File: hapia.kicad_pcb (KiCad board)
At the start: 6 copper layers, 19 parts, among them J1 ATX-20, J3 Conn_01x04_Pin, J4 Conn_01x04_Pin, J5 Conn_01x04_Pin, J6 Conn_01x04_Pin, J7 Conn_01x15_Pin, J8 SUB_placa_de_controle, U1 STM32F407VETx, U2 TMC2209-LA, U3 TPS54302, U4 TMC2209-LA, U5 TMC2209-LA, U6 TMC2209-LA, U7 SRV05-4

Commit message: 21082026/G
falta muita coisa
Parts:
- moved U1 74.4 mm to (74.5, 74.3)

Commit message: 29082026/I
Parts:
- removed J1: ATX-20, Connector_Molex:Molex_Mini-Fit_Jr_5566-20A_2x10_P4.20mm_Vertical
- removed J8: SUB_placa_de_controle, Connector_PinHeader_2.54mm:PinHeader_1x10_P2.54mm_Vertical
- removed L1: 6.8uh, Inductor_SMD:L_Bourns_SRP1038C_10.0x10.0mm
- added C1: 22pf, Capacitor_SMD:C_0603_1608Metric_Pad1.08x0.95mm_HandSolder, F.Cu at (59.1, 84.2)
- added C12: 1µf, Capacitor_SMD:C_0805_2012Metric_Pad1.18x1.45mm_HandSolder, F.Cu at (78.6, 21.0)
- added C13: 100nf, Capacitor_SMD:C_0603_1608Metric, F.Cu at (38.9, 54.1)
- added C15: 22nf, Capacitor_SMD:C_0603_1608Metric_Pad1.08x0.95mm_HandSolder, F.Cu at (59.1, 89.2)
- added C16: 22nf, Capacitor_SMD:C_0603_1608Metric_Pad1.08x0.95mm_HandSolder, F.Cu at (59.1, 91.8)
- added C17: 100nf, Capacitor_SMD:C_0603_1608Metric, F.Cu at (38.9, 56.6)
- added C18: 100nf, Capacitor_SMD:C_0603_1608Metric, F.Cu at (38.9, 59.1)
- added C19: 100nf, Capacitor_SMD:C_0603_1608Metric, F.Cu at (38.9, 61.6)
- added C20: 100nf, Capacitor_SMD:C_0603_1608Metric, F.Cu at (38.9, 64.1)
- added C21: 1µf, Capacitor_SMD:C_0805_2012Metric_Pad1.18x1.45mm_HandSolder, F.Cu at (78.6, 24.0)
- added C22: 100nf, Capacitor_SMD:C_0603_1608Metric, F.Cu at (38.9, 66.6)
- added C23: 1µf, Capacitor_SMD:C_0805_2012Metric_Pad1.18x1.45mm_HandSolder, F.Cu at (78.6, 27.0)
- added C24: 100nf, Capacitor_SMD:C_0603_1608Metric, F.Cu at (42.9, 44.1)
- added C27: 1000µf, Capacitor_THT:CP_Radial_D12.5mm_P5.00mm, F.Cu at (27.4, 49.8)
- added C28: 100nf, Capacitor_SMD:C_0603_1608Metric, F.Cu at (42.9, 46.6)
- added C3: 100nf, Capacitor_SMD:C_0603_1608Metric, F.Cu at (38.9, 44.1)
- added C30: 100nf, Capacitor_SMD:C_0603_1608Metric, F.Cu at (42.9, 49.1)
- added C34: 1000µf, Capacitor_THT:CP_Radial_D12.5mm_P5.00mm, F.Cu at (27.4, 63.9)
- added C35: 22nf, Capacitor_SMD:C_0603_1608Metric_Pad1.08x0.95mm_HandSolder, F.Cu at (59.1, 94.3)
- added C36: 22nf, Capacitor_SMD:C_0603_1608Metric_Pad1.08x0.95mm_HandSolder, F.Cu at (59.1, 96.8)
- added C37: 100nf, Capacitor_SMD:C_0603_1608Metric, F.Cu at (42.9, 51.6)
- added C38: 100nf, Capacitor_SMD:C_0603_1608Metric, F.Cu at (42.9, 54.1)
- added C39: 100nf, Capacitor_SMD:C_0603_1608Metric, F.Cu at (42.9, 56.6)
- added C4: 100nf, Capacitor_SMD:C_0603_1608Metric, F.Cu at (38.9, 46.6)
- added C40: 100nf, Capacitor_SMD:C_0603_1608Metric, F.Cu at (42.9, 59.1)
- added C41: 1µf, Capacitor_SMD:C_0805_2012Metric_Pad1.18x1.45mm_HandSolder, F.Cu at (78.6, 30.0)
- added C42: 100nf, Capacitor_SMD:C_0603_1608Metric, F.Cu at (42.9, 61.6)
- added C43: 1µf, Capacitor_SMD:C_0805_2012Metric_Pad1.18x1.45mm_HandSolder, F.Cu at (78.6, 33.0)
- added C44: 100nf, Capacitor_SMD:C_0603_1608Metric, F.Cu at (42.9, 64.1)
- added C47: 100nf, Capacitor_SMD:C_0603_1608Metric, F.Cu at (42.9, 66.6)
- added C49: 100nf, Capacitor_SMD:C_0603_1608Metric, F.Cu at (46.9, 44.1)
- added C5: 22pf, Capacitor_SMD:C_0603_1608Metric_Pad1.08x0.95mm_HandSolder, F.Cu at (59.1, 86.7)
- added C54: 100nf, Capacitor_SMD:C_0603_1608Metric, F.Cu at (46.9, 46.6)
- added C56: 33nf, Capacitor_SMD:C_0402_1005Metric, F.Cu at (75.2, 89.7)
- added C57: 100nf, Capacitor_SMD:C_0603_1608Metric, F.Cu at (46.9, 49.1)
- added C58: 100nf, Capacitor_SMD:C_0603_1608Metric, F.Cu at (46.9, 51.6)
- added C59: 1000µf, Capacitor_THT:CP_Radial_D12.5mm_P5.00mm, F.Cu at (27.4, 77.9)
- added C60: 100nf, Capacitor_SMD:C_0603_1608Metric, F.Cu at (46.9, 54.1)
- added C61: 100nf, Capacitor_SMD:C_0603_1608Metric, F.Cu at (46.9, 56.6)
- added C63: 1µf, Capacitor_SMD:C_0805_2012Metric_Pad1.18x1.45mm_HandSolder, F.Cu at (78.6, 36.1)
- added C65: 100nf, Capacitor_SMD:C_0603_1608Metric, F.Cu at (46.9, 59.1)
- added C66: 1000µf, Capacitor_THT:CP_Radial_D12.5mm_P5.00mm, F.Cu at (27.4, 92.0)
- added C67: 100nf, Capacitor_SMD:C_0603_1608Metric, F.Cu at (46.9, 61.6)
- added C68: 100nf, Capacitor_SMD:C_0603_1608Metric, F.Cu at (46.9, 64.1)
- added C69: 100nf, Capacitor_SMD:C_0603_1608Metric, F.Cu at (46.9, 66.6)
- added C7: 100nf, Capacitor_SMD:C_0603_1608Metric, F.Cu at (38.9, 49.1)
- added C70: 100nf, Capacitor_SMD:C_0603_1608Metric, F.Cu at (50.9, 44.1)
- added C71: 100nf, Capacitor_SMD:C_0603_1608Metric, F.Cu at (50.9, 46.6)
- added C72: 100nf, Capacitor_SMD:C_0603_1608Metric, F.Cu at (50.9, 49.1)
- added C76: 100nf, Capacitor_SMD:C_0603_1608Metric, F.Cu at (50.9, 51.6)
- added C78: 100nf, Capacitor_SMD:C_0603_1608Metric, F.Cu at (50.9, 54.1)
- added C87: 100nf, Capacitor_SMD:C_0603_1608Metric, F.Cu at (50.9, 56.6)
- added C88: 100nf, Capacitor_SMD:C_0603_1608Metric, F.Cu at (50.9, 59.1)
- added C89: 100nf, Capacitor_SMD:C_0603_1608Metric, F.Cu at (50.9, 61.6)
- added C9: 100nf, Capacitor_SMD:C_0603_1608Metric, F.Cu at (38.9, 51.6)
- added C90: 100nf, Capacitor_SMD:C_0603_1608Metric, F.Cu at (50.9, 64.1)
- added C92: 100nf, Capacitor_SMD:C_0603_1608Metric, F.Cu at (50.9, 66.6)
- added C93: 100nf, Capacitor_SMD:C_0603_1608Metric, F.Cu at (54.9, 44.1)
- added C94: 100nf, Capacitor_SMD:C_0603_1608Metric, F.Cu at (54.9, 46.6)
- added CN1: 100nf, Capacitor_SMD:C_0603_1608Metric, F.Cu at (54.9, 49.1)
- added CN2: 100nf, Capacitor_SMD:C_0603_1608Metric, F.Cu at (54.9, 51.6)
- added CN3: 100nf, Capacitor_SMD:C_0603_1608Metric, F.Cu at (54.9, 54.1)
- added D1: SMF33A, Diode_SMD:D_SMF, F.Cu at (90.6, 69.2)
- added D3: SMF5V0A, Diode_SMD:D_SMF, F.Cu at (90.6, 72.5)
- added D4: SMF5V0A, Diode_SMD:D_SMF, F.Cu at (90.6, 75.9)
- added D7: SMF5V0A, Diode_SMD:D_SMF, F.Cu at (90.6, 79.2)
- added D8: SMF15A, Diode_SMD:D_SMF, F.Cu at (90.6, 82.6)
- added D9: SMF5V0A, Diode_SMD:D_SMF, F.Cu at (90.6, 85.9)
- added FB3: FerriteBead, Inductor_SMD:L_0805_2012Metric, F.Cu at (76.0, 87.4)
- added J17: Conn_01x04_MountingPin, Connector_JST:JST_SH_SM04B-SRSS-TB_1x04-1MP_P1.00mm_Horizontal, F.Cu at (92.1, 91.4)
- added J9: Conn_01x15_Pin, Connector_PinHeader_2.54mm:PinHeader_1x15_P2.54mm_Vertical, F.Cu at (59.2, 45.1)
- added JP1: usb/atx, Jumper:SolderJumper-3_P1.3mm_Bridged2Bar12_RoundedPad1.0x1.5mm, F.Cu at (39.7, 96.8)
- added JP2: fre, Jumper:SolderJumper-2_P1.3mm_Open_TrianglePad1.0x1.5mm, F.Cu at (44.7, 96.8)
- added R59: 100mΩ, Resistor_SMD:R_1206_3216Metric, F.Cu at (50.5, 69.6)
- added R60: 100mΩ, Resistor_SMD:R_1206_3216Metric, F.Cu at (50.5, 72.9)
- added R61: 100mΩ, Resistor_SMD:R_1206_3216Metric, F.Cu at (50.5, 76.2)
- added R62: 100mΩ, Resistor_SMD:R_1206_3216Metric, F.Cu at (50.5, 79.5)
- added R67: 100mΩ, Resistor_SMD:R_1206_3216Metric, F.Cu at (50.5, 82.8)
- added R68: 100mΩ, Resistor_SMD:R_1206_3216Metric, F.Cu at (50.5, 86.1)
- added R69: 100mΩ, Resistor_SMD:R_1206_3216Metric, F.Cu at (50.5, 89.4)
- added R70: 100mΩ, Resistor_SMD:R_1206_3216Metric, F.Cu at (50.5, 92.7)
- added TP10: 3.3v_power, TestPoint:TestPoint_Pad_D1.0mm, F.Cu at (69.2, 90.6)
- added TP11: 12v_power, TestPoint:TestPoint_Pad_D1.0mm, F.Cu at (69.2, 93.6)
- added TP12: 12v_power, TestPoint:TestPoint_Pad_D1.0mm, F.Cu at (69.2, 96.7)
- added TP13: TestPoint, TestPoint:TestPoint_Pad_D1.0mm, F.Cu at (72.2, 87.5)
- added TP14: 12v, TestPoint:TestPoint_Pad_D1.0mm, F.Cu at (72.2, 90.6)
- added TP15: 5v, TestPoint:TestPoint_Pad_D1.0mm, F.Cu at (72.2, 93.6)
- added TP16: 3.3v, TestPoint:TestPoint_Pad_D1.0mm, F.Cu at (72.2, 96.7)
- added TP5: 3.3v_power, TestPoint:TestPoint_Pad_D1.0mm, F.Cu at (66.1, 87.5)
- added TP6: 3.3v_power, TestPoint:TestPoint_Pad_D1.0mm, F.Cu at (66.1, 90.6)
- added TP7: 12v_power, TestPoint:TestPoint_Pad_D1.0mm, F.Cu at (66.1, 93.6)
- added TP8: 12v_power, TestPoint:TestPoint_Pad_D1.0mm, F.Cu at (66.1, 96.7)
- added TP9: 3.3v_power, TestPoint:TestPoint_Pad_D1.0mm, F.Cu at (69.2, 87.5)
- added U10: 74HC4051, Package_DIP:DIP-16_W7.62mm, F.Cu at (38.5, 69.9)
- added U11: UCC27524DR, Package_SO:SOIC-8_3.9x4.9mm_P1.27mm, F.Cu at (85.2, 22.9)
- added U12: UCC27524D, Package_SO:SOIC-8_3.9x4.9mm_P1.27mm, F.Cu at (85.2, 29.4)
- added U13: IRFS7530TRL7PP, Package_TO_SOT_SMD:TO-263-7_TabPin4, F.Cu at (72.3, 49.0)
- added U14: IRFS7530TRL7PP, Package_TO_SOT_SMD:TO-263-7_TabPin4, F.Cu at (72.3, 61.3)
- added U8: TPS62933F, Package_TO_SOT_SMD:SOT-583-8, F.Cu at (78.0, 39.6)
- added U9: SRV05-4, Package_TO_SOT_SMD:SOT-23-6, F.Cu at (93.4, 39.7)
- added Y1: 8mhz, Crystal:Crystal_SMD_5032-2Pin_5.0x3.2mm_HandSoldering, F.Cu at (42.1, 92.4)
- J7: value Conn_01x15_Pin -> ATX-24; footprint Connector_PinSocket_2.54mm:PinSocket_1x15_P2.54mm_Vertical -> Connector_Molex:Molex_Mini-Fit_Jr_5569-24A2_2x12_P4.20mm_Horizontal
- TP1, TP2, TP4: footprint Connector_USB:USB_Micro-B_Amphenol_10104110_Horizontal -> TestPoint:TestPoint_Pad_D1.0mm
- TP3: value TestPoint -> 3.3v; footprint Connector_USB:USB_Micro-B_Amphenol_10104110_Horizontal -> TestPoint:TestPoint_Pad_D1.0mm
- U1: value STM32F407VETx -> STM32F407VET6
- U2: value TMC2209-LA -> AMS1117-3.3; footprint Package_DFN_QFN:VQFN-28-1EP_5x5mm_P0.5mm_EP3.7x3.7mm_ThermalVias -> Package_TO_SOT_SMD:SOT-223-3_TabPin2
- U3: value TPS54302 -> SRV05-4
- U7: value SRV05-4 -> TMC2209-LA; footprint Package_TO_SOT_SMD:SOT-23-6 -> Package_DFN_QFN:VQFN-28-1EP_5x5mm_P0.5mm_EP3.7x3.7mm_ThermalVias
- moved U4 68.6 mm to (84.0, 71.1)
- moved U5 68.6 mm to (84.0, 78.4)
- moved U6 68.6 mm to (84.0, 85.6)
- moved TP1 66.8 mm to (63.1, 87.5)
- moved U1 64.9 mm to (139.0, 80.8), turned to 45 degrees
- moved TP2 64.4 mm to (63.1, 90.6)
- moved TP3 62.5 mm to (63.1, 93.6)
- moved U7 61.4 mm to (84.0, 92.9)
- moved U2 61.0 mm to (85.9, 36.9)
- moved TP4 60.9 mm to (63.1, 96.7)
- moved J3 54.2 mm to (82.8, 45.4)
- moved J4 54.2 mm to (82.8, 51.3)
- moved J5 54.2 mm to (82.8, 57.1)
- moved J6 54.2 mm to (82.8, 63.0)
- moved U3 49.2 mm to (93.4, 35.1)
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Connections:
- net Net-(U1-PA7) renamed SUB_RMII_CRS_DV
- net Net-(U3-BOOT) renamed USB_C_D-
- net Net-(U3-FB) renamed USB_C_D+
- net exrtusora renamed SWD_SWO
- net gpi_4 renamed Net-(J7-+5VSB)
- net gpi_5 renamed ATX_PWR
- J7 pad 1: GND -> unconnected-(J7-+3.3V-Pad1)_2
- J7 pad 10: gpi_3 -> hotbed
- J7 pad 11: gpi_2 -> hotbed
- J7 pad 12: gpi_1 -> unconnected-(J7-+3.3V-Pad1)_3
- J7 pad 13: +5V -> unconnected-(J7-+3.3V-Pad1)
- J7 pad 14: Net-(J7-Pin_14) -> unconnected-(J7--12V-Pad14)
- J7 pad 15: +12V -> GND
- J7 pad 2: STM_ADC -> unconnected-(J7-+3.3V-Pad1)_1
- J7 pad 3: STM_ADC_1 -> GND
- J7 pad 4: GND -> Net-(F7-Pad1)
- J7 pad 5: gpi_8 -> GND
- J7 pad 6: gpi_7 -> Net-(F7-Pad1)
- J7 pad 7: gpi_6 -> GND
- TP1 pad 1: 3.3v/1 -> STM_boot
- TP2 pad 1: 3.3v/1 -> STM_nrst
- TP4 pad 1: +12V -> Net-(D2-A)
- U1 pad 1: unconnected-(U1-PE2-Pad1) -> Net-(U1-PE2)
- U1 pad 14: 3.3v/1 -> STM_nrst
- U1 pad 15: unconnected-(U1-PC0-Pad15) -> NTC_MUX_out
- U1 pad 17: unconnected-(U1-PC2-Pad17) -> Net-(RN4A-R1.2)
- U1 pad 18: unconnected-(U1-PC3-Pad18) -> Net-(RN4B-R2.2)
- U1 pad 2: unconnected-(U1-PE3-Pad2) -> Net-(U1-PE3)
- U1 pad 21: 3.3v/A -> VDDA
- U1 pad 22: Net-(U1-VDDA) -> VDDA
- U1 pad 3: unconnected-(U1-PE4-Pad3) -> Net-(U1-PE4)
- U1 pad 36: unconnected-(U1-PB1-Pad36) -> SWD/jtag_rst
- U1 pad 38: unconnected-(U1-PE7-Pad38) -> Net-(RN3A-R1.1)
- U1 pad 39: unconnected-(U1-PE8-Pad39) -> Net-(RN3B-R2.1)
- U1 pad 4: unconnected-(U1-PE5-Pad4) -> Net-(U1-PE5)
- U1 pad 40: unconnected-(U1-PE9-Pad40) -> Net-(RN3C-R3.1)
- U1 pad 41: unconnected-(U1-PE10-Pad41) -> Net-(RN3D-R4.1)
- U1 pad 42: unconnected-(U1-PE11-Pad42) -> Net-(RN3E-R5.1)
- U1 pad 43: unconnected-(U1-PE12-Pad43) -> Net-(RN3F-R6.1)
- U1 pad 44: unconnected-(U1-PE13-Pad44) -> Net-(RN3G-R7.1)
- U1 pad 45: unconnected-(U1-PE14-Pad45) -> Net-(RN3H-R8.1)
- U1 pad 46: unconnected-(U1-PE15-Pad46) -> Net-(U1-PE15)
- U1 pad 48: unconnected-(U1-PB11-Pad48) -> Net-(U1-PB11)
- U1 pad 5: unconnected-(U1-PE6-Pad5) -> Net-(U1-PE6)
- U1 pad 51: unconnected-(U1-PB12-Pad51) -> Net-(U1-PB12)
- U1 pad 52: unconnected-(U1-PB13-Pad52) -> Net-(U1-PB13)
- U1 pad 55: unconnected-(U1-PD8-Pad55) -> NTC_MUX_0
- U1 pad 56: unconnected-(U1-PD9-Pad56) -> NTC_MUX_1
- U1 pad 57: unconnected-(U1-PD10-Pad57) -> NTC_MUX_2
- U1 pad 61: unconnected-(U1-PD14-Pad61) -> Net-(U1-PD14)
- U1 pad 62: unconnected-(U1-PD15-Pad62) -> Net-(U1-PD15)
- U1 pad 63: unconnected-(U1-PC6-Pad63) -> Net-(RN4E-R5.2)
- U1 pad 64: unconnected-(U1-PC7-Pad64) -> Net-(RN4F-R6.2)
- U1 pad 65: unconnected-(U1-PC8-Pad65) -> Net-(RN4G-R7.2)
- U1 pad 66: unconnected-(U1-PC9-Pad66) -> Net-(RN4H-R8.2)
- U1 pad 70: unconnected-(U1-PA11-Pad70) -> gpi_PD14
- U1 pad 71: unconnected-(U1-PA12-Pad71) -> gpi_PD15
- U1 pad 72: unconnected-(U1-PA13-Pad72) -> Net-(U1-PA13)
- U1 pad 76: unconnected-(U1-PA14-Pad76) -> Net-(U1-PA14)
- U1 pad 77: Net-(U1-PA15) -> unconnected-(U1-PA15-Pad77)
- U1 pad 78: Net-(U1-PC10) -> unconnected-(U1-PC10-Pad78)
- U1 pad 79: Net-(U1-PC11) -> unconnected-(U1-PC11-Pad79)
- U1 pad 91: SUB_2 -> Net-(RN1G-R7.2)
- U1 pad 92: SUB_3 -> Net-(RN1F-R6.2)
- U1 pad 93: SUB_4 -> Net-(RN1E-R5.2)
- U1 pad 94: 3.3v/1 -> STM_boot
- U1 pad 95: SUB_5 -> Net-(RN1D-R4.2)
- U1 pad 96: SUB_6 -> Net-(RN1C-R3.2)
- U1 pad 97: unconnected-(U1-PE0-Pad97) -> Net-(RN1A-R1.1)
- U1 pad 98: unconnected-(U1-PE1-Pad98) -> Net-(RN1B-R2.1)
- U2 pad 1: Net-(J3-Pin_1) -> GND
- U2 pad 2: Net-(U2-~{EN}) -> +3.3Vdev
- U2 pad 3: GND -> +5Vusb
- U3 pad 1: GND -> unconnected-(U3-IO1-Pad1)
- U3 pad 2: Net-(U3-SW) -> Net-(D2-A)
- U3 pad 3: Net-(U3-VIN) -> unconnected-(U3-IO2-Pad3)
- U3 pad 5: unconnected-(U3-EN-Pad5) -> GND
- U4 pad 1: Net-(J4-Pin_1) -> Net-(J3-Pin_1)
- U4 pad 10: TMC_MS2_3 -> GND
- U4 pad 14: TMC_uart3 -> TMC_uart
- U4 pad 15: 3.3v/1 -> +3V3
- U4 pad 16: unconnected-(U4-STEP-Pad16) -> TMC_step_1
- U4 pad 17: unconnected-(U4-VREF-Pad17) -> Net-(U4-VREF)
- U4 pad 19: unconnected-(U4-DIR-Pad19) -> TMC_DIR_1
- U4 pad 21: Net-(J4-Pin_3) -> Net-(J3-Pin_3)
- U4 pad 22: +12V -> +12P
- U4 pad 24: Net-(J4-Pin_4) -> Net-(J3-Pin_4)
- U4 pad 26: Net-(J4-Pin_2) -> Net-(J3-Pin_2)
- U4 pad 28: +12V -> +12P
- U4 pad 6: TMC_3vcp -> Net-(U4-VCP)
- U4 pad 8: TMC_3vut -> Net-(U4-5VOUT)
- U4 pad 9: TMC_MS1_3 -> GND
- U5 pad 1: Net-(J5-Pin_1) -> Net-(J4-Pin_1)
- U5 pad 10: TMC_MS2_4 -> GND
- U5 pad 14: TMC_uart4 -> TMC_uart
- U5 pad 15: 3.3v/1 -> +3V3
- U5 pad 16: unconnected-(U5-STEP-Pad16) -> TMC_step_3
- U5 pad 17: unconnected-(U5-VREF-Pad17) -> Net-(U5-VREF)
- U5 pad 19: unconnected-(U5-DIR-Pad19) -> TMC_DIR_3
- U5 pad 21: Net-(J5-Pin_3) -> Net-(J4-Pin_3)
- U5 pad 22: +12V -> +12P
- U5 pad 24: Net-(J5-Pin_4) -> Net-(J4-Pin_4)
- U5 pad 26: Net-(J5-Pin_2) -> Net-(J4-Pin_2)
- U5 pad 28: +12V -> +12P
- U5 pad 6: TMC_4vcp -> Net-(U5-VCP)
- U5 pad 8: TMC_4vut -> Net-(U5-5VOUT)
- U5 pad 9: TMC_MS1_4 -> +3V3
- U6 pad 1: Net-(J6-Pin_1) -> Net-(J5-Pin_1)
- U6 pad 10: TMC_MS2_2 -> +3V3
- U6 pad 14: TMC_uart2 -> TMC_uart
- U6 pad 15: 3.3v/1 -> +3V3
- U6 pad 16: unconnected-(U6-STEP-Pad16) -> TMC_step_2
- U6 pad 17: unconnected-(U6-VREF-Pad17) -> Net-(U6-VREF)
- U6 pad 19: unconnected-(U6-DIR-Pad19) -> TMC_DIR_2
- U6 pad 21: Net-(J6-Pin_3) -> Net-(J5-Pin_3)
- U6 pad 22: +12V -> +12P
- U6 pad 24: Net-(J6-Pin_4) -> Net-(J5-Pin_4)
- U6 pad 26: Net-(J6-Pin_2) -> Net-(J5-Pin_2)
- U6 pad 28: +12V -> +12P
- U6 pad 6: TMC_2vcp -> Net-(U6-VCP)
- U6 pad 8: TMC_2vut -> Net-(U6-5VOUT)
- U6 pad 9: TMC_MS1_2 -> GND
- U7 pad 1: unconnected-(U7-IO1-Pad1) -> Net-(J6-Pin_1)
- U7 pad 2: unconnected-(U7-VN-Pad2) -> Net-(U7-~{EN})
- U7 pad 3: Net-(U7-IO2) -> GND
- U7 pad 4: unconnected-(U7-IO3-Pad4) -> Net-(U7-CPO)
- U7 pad 5: unconnected-(U7-VP-Pad5) -> Net-(U7-CPI)
- U7 pad 6: unconnected-(U7-IO4-Pad6) -> Net-(U7-VCP)

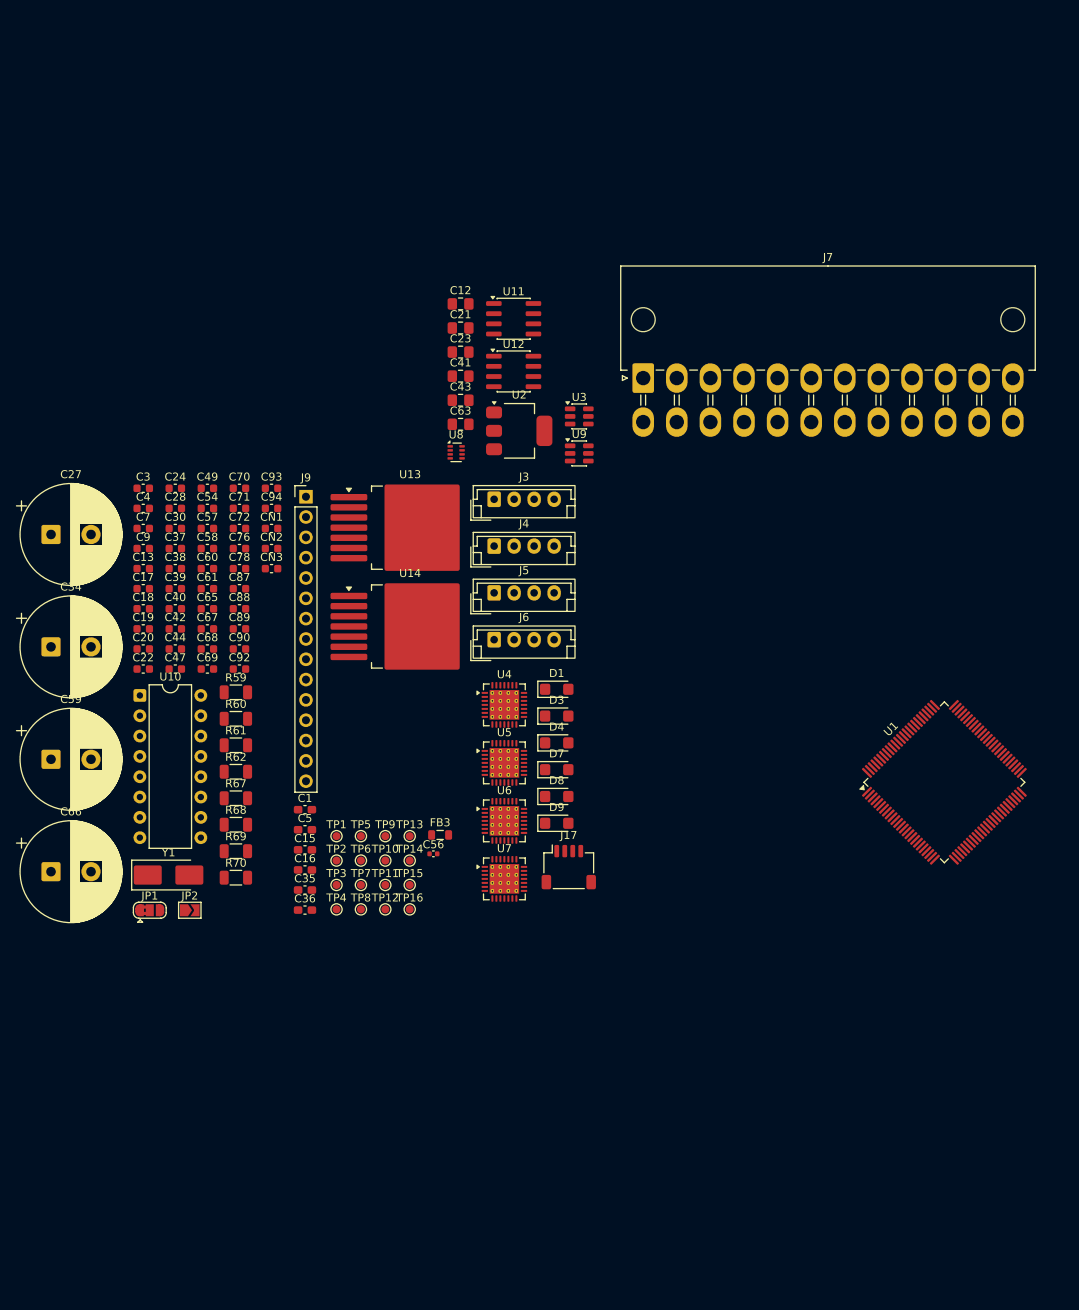
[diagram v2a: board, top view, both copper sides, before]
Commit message: o .bom não foi terminado
O desafio e todo custar menos de 150 dólares(eua) e menos de 1000r(reais)
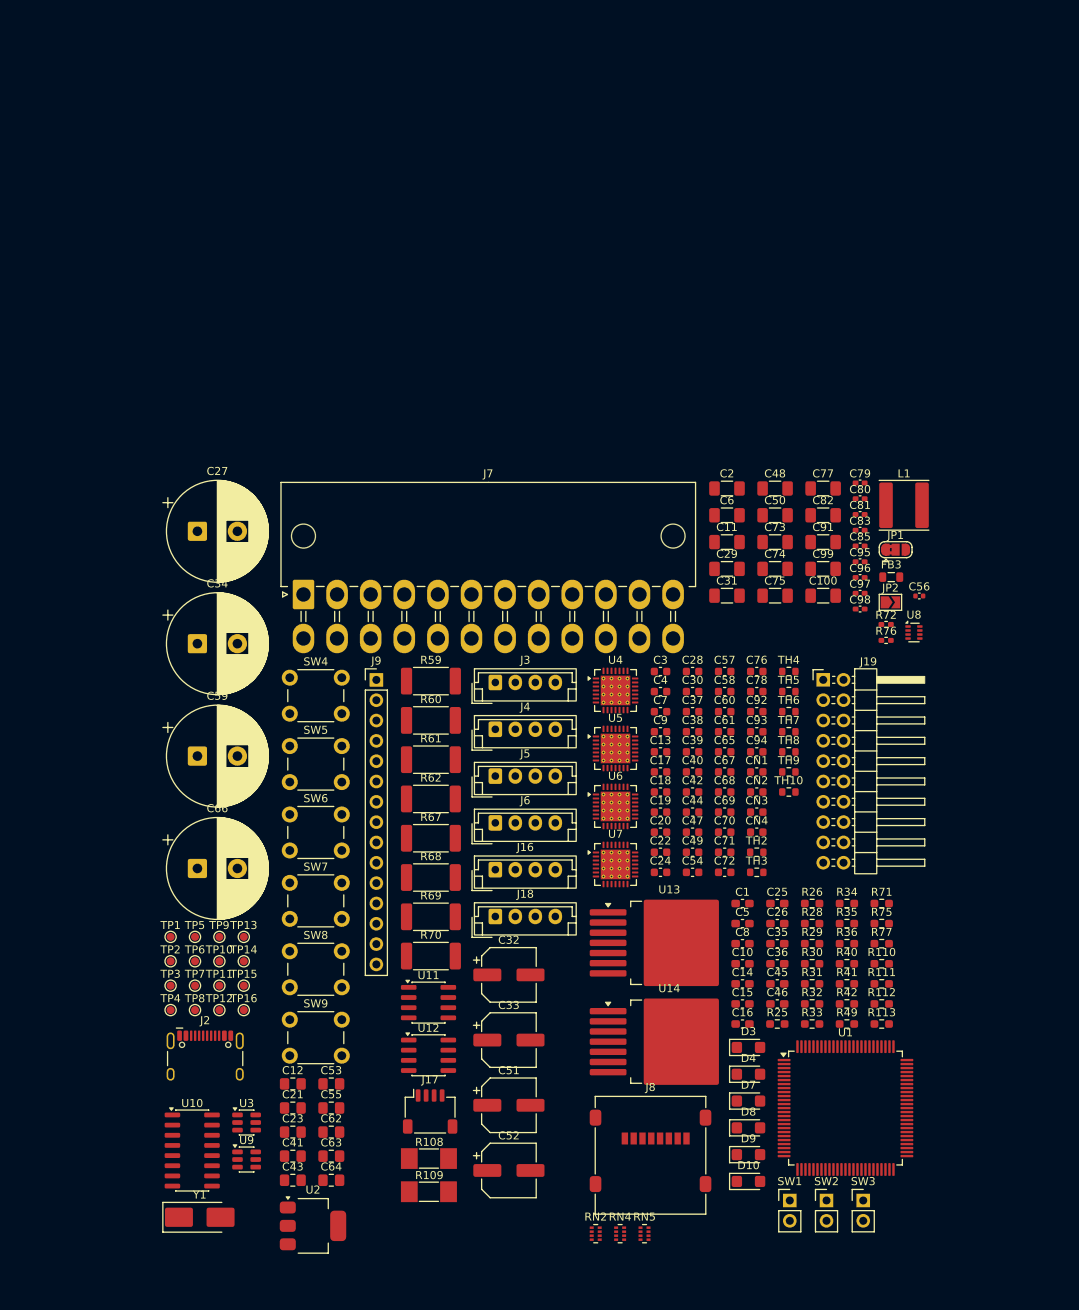
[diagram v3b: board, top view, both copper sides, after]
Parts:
- removed C87, C88, C89, C90: 100nf, Capacitor_SMD:C_0603_1608Metric
- removed D1: SMF33A, Diode_SMD:D_SMF
- added C10: 4.7µf, Capacitor_SMD:C_0603_1608Metric_Pad1.08x0.95mm_HandSolder, F.Cu at (113.8, 103.5)
- added C100: 10µf, Capacitor_SMD:C_1206_3216Metric_Pad1.33x1.80mm_HandSolder, F.Cu at (123.9, 57.5)
- added C11: 10µf, Capacitor_SMD:C_1206_3216Metric_Pad1.33x1.80mm_HandSolder, F.Cu at (111.9, 50.8)
- added C14: 4.7µf, Capacitor_SMD:C_0603_1608Metric_Pad1.08x0.95mm_HandSolder, F.Cu at (113.8, 106.0)
- added C2: 10µf, Capacitor_SMD:C_1206_3216Metric_Pad1.33x1.80mm_HandSolder, F.Cu at (111.9, 44.1)
- added C25: 4.7µf, Capacitor_SMD:C_0603_1608Metric_Pad1.08x0.95mm_HandSolder, F.Cu at (118.2, 96.0)
- added C26: 4.7µf, Capacitor_SMD:C_0603_1608Metric_Pad1.08x0.95mm_HandSolder, F.Cu at (118.2, 98.5)
- added C29: 10µf, Capacitor_SMD:C_1206_3216Metric_Pad1.33x1.80mm_HandSolder, F.Cu at (111.9, 54.1)
- added C31: 10µf, Capacitor_SMD:C_1206_3216Metric_Pad1.33x1.80mm_HandSolder, F.Cu at (111.9, 57.5)
- added C32: 100µf, Capacitor_SMD:CP_Elec_6.3x7.7, F.Cu at (84.6, 104.9)
- added C33: 100µf, Capacitor_SMD:CP_Elec_6.3x7.7, F.Cu at (84.6, 113.0)
- added C45: 4.7µf, Capacitor_SMD:C_0603_1608Metric_Pad1.08x0.95mm_HandSolder, F.Cu at (118.2, 106.0)
- added C46: 4.7µf, Capacitor_SMD:C_0603_1608Metric_Pad1.08x0.95mm_HandSolder, F.Cu at (118.2, 108.5)
- added C48: 10µf, Capacitor_SMD:C_1206_3216Metric_Pad1.33x1.80mm_HandSolder, F.Cu at (117.9, 44.1)
- added C50: 10µf, Capacitor_SMD:C_1206_3216Metric_Pad1.33x1.80mm_HandSolder, F.Cu at (117.9, 47.4)
- added C51: 100µf, Capacitor_SMD:CP_Elec_6.3x7.7, F.Cu at (84.6, 121.2)
- added C52: 100µf, Capacitor_SMD:CP_Elec_6.3x7.7, F.Cu at (84.6, 129.3)
- added C53: 22µf, Capacitor_SMD:C_0805_2012Metric_Pad1.18x1.45mm_HandSolder, F.Cu at (62.4, 118.5)
- added C55: 22µf, Capacitor_SMD:C_0805_2012Metric_Pad1.18x1.45mm_HandSolder, F.Cu at (62.4, 121.5)
- added C6: 10µf, Capacitor_SMD:C_1206_3216Metric_Pad1.33x1.80mm_HandSolder, F.Cu at (111.9, 47.4)
- added C62: 22µf, Capacitor_SMD:C_0805_2012Metric_Pad1.18x1.45mm_HandSolder, F.Cu at (62.4, 124.5)
- added C64: 22µf, Capacitor_SMD:C_0805_2012Metric_Pad1.18x1.45mm_HandSolder, F.Cu at (62.4, 130.5)
- added C73: 10µf, Capacitor_SMD:C_1206_3216Metric_Pad1.33x1.80mm_HandSolder, F.Cu at (117.9, 50.8)
- added C74: 10µf, Capacitor_SMD:C_1206_3216Metric_Pad1.33x1.80mm_HandSolder, F.Cu at (117.9, 54.1)
- added C75: 10µf, Capacitor_SMD:C_1206_3216Metric_Pad1.33x1.80mm_HandSolder, F.Cu at (117.9, 57.5)
- added C77: 10µf, Capacitor_SMD:C_1206_3216Metric_Pad1.33x1.80mm_HandSolder, F.Cu at (123.9, 44.1)
- added C79: 10nf, Capacitor_SMD:C_0402_1005Metric_Pad0.74x0.62mm_HandSolder, F.Cu at (128.5, 43.4)
- added C8: 4.7µf, Capacitor_SMD:C_0603_1608Metric_Pad1.08x0.95mm_HandSolder, F.Cu at (113.8, 101.0)
- added C80: 10nf, Capacitor_SMD:C_0402_1005Metric_Pad0.74x0.62mm_HandSolder, F.Cu at (128.5, 45.4)
- added C81: 10nf, Capacitor_SMD:C_0402_1005Metric_Pad0.74x0.62mm_HandSolder, F.Cu at (128.5, 47.3)
- added C82: 10µf, Capacitor_SMD:C_1206_3216Metric_Pad1.33x1.80mm_HandSolder, F.Cu at (123.9, 47.4)
- added C83: 10nf, Capacitor_SMD:C_0402_1005Metric_Pad0.74x0.62mm_HandSolder, F.Cu at (128.5, 49.3)
- added C85: 10nf, Capacitor_SMD:C_0402_1005Metric_Pad0.74x0.62mm_HandSolder, F.Cu at (128.5, 51.3)
- added C91: 10µf, Capacitor_SMD:C_1206_3216Metric_Pad1.33x1.80mm_HandSolder, F.Cu at (123.9, 50.8)
- added C95: 10nf, Capacitor_SMD:C_0402_1005Metric_Pad0.74x0.62mm_HandSolder, F.Cu at (128.5, 53.2)
- added C96: 10nf, Capacitor_SMD:C_0402_1005Metric_Pad0.74x0.62mm_HandSolder, F.Cu at (128.5, 55.2)
- added C97: 10nf, Capacitor_SMD:C_0402_1005Metric_Pad0.74x0.62mm_HandSolder, F.Cu at (128.5, 57.2)
- added C98: 10nf, Capacitor_SMD:C_0402_1005Metric_Pad0.74x0.62mm_HandSolder, F.Cu at (128.5, 59.1)
- added C99: 10µf, Capacitor_SMD:C_1206_3216Metric_Pad1.33x1.80mm_HandSolder, F.Cu at (123.9, 54.1)
- added CN4: 100nf, Capacitor_SMD:C_0603_1608Metric, F.Cu at (115.6, 87.0)
- added D10: SMF12A, Diode_SMD:D_SMF, F.Cu at (114.6, 130.7)
- added J16: Conn_01x04_Pin, Connector_JST:JST_EH_B4B-EH-A_1x04_P2.50mm_Vertical, F.Cu at (82.9, 91.7)
- added J18: Conn_01x04_Pin, Connector_JST:JST_EH_B4B-EH-A_1x04_P2.50mm_Vertical, F.Cu at (82.9, 97.6)
- added J19: ETH, Connector_PinHeader_2.54mm:PinHeader_2x10_P2.54mm_Horizontal, F.Cu at (123.9, 68.0)
- added J2: USB_C_Receptacle_USB2.0_16P, Connector_USB:USB_C_Receptacle_HCTL_HC-TYPE-C-16P-01A, F.Cu at (46.6, 116.2)
- added J8: Micro_SD_Card, Connector_Card:microSD_HC_Molex_47219-2001, F.Cu at (102.3, 127.4)
- added L1: 4.7µh, Inductor_SMD:L_Changjiang_FNR6020S, F.Cu at (134.0, 46.2)
- added R108: 12Ω, Resistor_SMD:R_MELF_MMB-0207, F.Cu at (74.6, 127.8)
- added R109: 12Ω, Resistor_SMD:R_MELF_MMB-0207, F.Cu at (74.6, 132.0)
- added R110: 33Ω, Resistor_SMD:R_0603_1608Metric_Pad0.98x0.95mm_HandSolder, F.Cu at (131.2, 103.5)
- added R111: 33Ω, Resistor_SMD:R_0603_1608Metric_Pad0.98x0.95mm_HandSolder, F.Cu at (131.2, 106.0)
- added R112: 33Ω, Resistor_SMD:R_0603_1608Metric_Pad0.98x0.95mm_HandSolder, F.Cu at (131.2, 108.5)
- added R113: 33Ω, Resistor_SMD:R_0603_1608Metric_Pad0.98x0.95mm_HandSolder, F.Cu at (131.2, 111.0)
- added R25: 22Ω, Resistor_SMD:R_0603_1608Metric_Pad0.98x0.95mm_HandSolder, F.Cu at (118.2, 111.0)
- added R26: 22Ω, Resistor_SMD:R_0603_1608Metric_Pad0.98x0.95mm_HandSolder, F.Cu at (122.5, 96.0)
- added R28: 33Ω, Resistor_SMD:R_0603_1608Metric_Pad0.98x0.95mm_HandSolder, F.Cu at (122.5, 98.5)
- added R29: 33Ω, Resistor_SMD:R_0603_1608Metric_Pad0.98x0.95mm_HandSolder, F.Cu at (122.5, 101.0)
- added R30: 33Ω, Resistor_SMD:R_0603_1608Metric_Pad0.98x0.95mm_HandSolder, F.Cu at (122.5, 103.5)
- added R31: 33Ω, Resistor_SMD:R_0603_1608Metric_Pad0.98x0.95mm_HandSolder, F.Cu at (122.5, 106.0)
- added R32: 33Ω, Resistor_SMD:R_0603_1608Metric_Pad0.98x0.95mm_HandSolder, F.Cu at (122.5, 108.5)
- added R33: 33Ω, Resistor_SMD:R_0603_1608Metric_Pad0.98x0.95mm_HandSolder, F.Cu at (122.5, 111.0)
- added R34: 33Ω, Resistor_SMD:R_0603_1608Metric_Pad0.98x0.95mm_HandSolder, F.Cu at (126.9, 96.0)
- added R35: 33Ω, Resistor_SMD:R_0603_1608Metric_Pad0.98x0.95mm_HandSolder, F.Cu at (126.9, 98.5)
- added R36: 33Ω, Resistor_SMD:R_0603_1608Metric_Pad0.98x0.95mm_HandSolder, F.Cu at (126.9, 101.0)
- added R40: 33Ω, Resistor_SMD:R_0603_1608Metric_Pad0.98x0.95mm_HandSolder, F.Cu at (126.9, 103.5)
- added R41: 33Ω, Resistor_SMD:R_0603_1608Metric_Pad0.98x0.95mm_HandSolder, F.Cu at (126.9, 106.0)
- added R42: 33Ω, Resistor_SMD:R_0603_1608Metric_Pad0.98x0.95mm_HandSolder, F.Cu at (126.9, 108.5)
- added R49: 33Ω, Resistor_SMD:R_0603_1608Metric_Pad0.98x0.95mm_HandSolder, F.Cu at (126.9, 111.0)
- added R71: 100kΩ, Resistor_SMD:R_0603_1608Metric_Pad0.98x0.95mm_HandSolder, F.Cu at (131.2, 96.0)
- added R72: 57.6kΩ, Resistor_SMD:R_0402_1005Metric_Pad0.72x0.64mm_HandSolder, F.Cu at (131.8, 61.1)
- added R75: 33Ω, Resistor_SMD:R_0603_1608Metric_Pad0.98x0.95mm_HandSolder, F.Cu at (131.2, 98.5)
- added R76: 330Ω, Resistor_SMD:R_0402_1005Metric_Pad0.72x0.64mm_HandSolder, F.Cu at (131.8, 63.1)
- added R77: 30.9kΩ, Resistor_SMD:R_0603_1608Metric_Pad0.98x0.95mm_HandSolder, F.Cu at (131.2, 101.0)
- added RN2: 33Ω, Resistor_SMD:R_Array_Concave_4x0402, F.Cu at (95.5, 137.2)
- added RN4: 33Ω, Resistor_SMD:R_Array_Concave_4x0402, F.Cu at (98.5, 137.2)
- added RN5: 33Ω, Resistor_SMD:R_Array_Concave_4x0402, F.Cu at (101.6, 137.2)
- added SW1: SW_Push, Connector_PinHeader_2.54mm:PinHeader_1x02_P2.54mm_Vertical, F.Cu at (119.7, 133.1)
- added SW2: SW_Push, Connector_PinHeader_2.54mm:PinHeader_1x02_P2.54mm_Vertical, F.Cu at (124.3, 133.1)
- added SW3: SW_Push, Connector_PinHeader_2.54mm:PinHeader_1x02_P2.54mm_Vertical, F.Cu at (128.9, 133.1)
- added SW4: SW_P, Button_Switch_THT:SW_PUSH_6mm_H5mm, F.Cu at (57.2, 67.7)
- added SW5: SW_P, Button_Switch_THT:SW_PUSH_6mm_H5mm, F.Cu at (57.2, 76.3)
- added SW6: SW_P, Button_Switch_THT:SW_PUSH_6mm_H5mm, F.Cu at (57.2, 84.8)
- added SW7: SW_P, Button_Switch_THT:SW_PUSH_6mm_H5mm, F.Cu at (57.2, 93.4)
- added SW8: SW_P, Button_Switch_THT:SW_PUSH_6mm_H5mm, F.Cu at (57.2, 101.9)
- added SW9: SW_P, Button_Switch_THT:SW_PUSH_6mm_H5mm, F.Cu at (57.2, 110.5)
- added TH10: 10kΩ, Resistor_SMD:R_0603_1608Metric, F.Cu at (119.6, 82.0)
- added TH2: 10kΩ, Resistor_SMD:R_0603_1608Metric, F.Cu at (115.6, 89.5)
- added TH3: 10kΩ, Resistor_SMD:R_0603_1608Metric, F.Cu at (115.6, 92.1)
- added TH4: 10kΩ, Resistor_SMD:R_0603_1608Metric, F.Cu at (119.6, 67.0)
- added TH5: 10kΩ, Resistor_SMD:R_0603_1608Metric, F.Cu at (119.6, 69.5)
- added TH6: 10kΩ, Resistor_SMD:R_0603_1608Metric, F.Cu at (119.6, 72.0)
- added TH7: 10kΩ, Resistor_SMD:R_0603_1608Metric, F.Cu at (119.6, 74.5)
- added TH8: 10kΩ, Resistor_SMD:R_0603_1608Metric, F.Cu at (119.6, 77.0)
- added TH9: 10kΩ, Resistor_SMD:R_0603_1608Metric, F.Cu at (119.6, 79.5)
- D4, D7, D9: value SMF5V0A -> SMF3.3
- D8: value SMF15A -> SMF3.3
- R59, R60, R61, R62, R67, R68, R69, R70: footprint Resistor_SMD:R_1206_3216Metric -> Resistor_SMD:R_2512_6332Metric_Pad1.40x3.35mm_HandSolder
- U10: footprint Package_DIP:DIP-16_W7.62mm -> Package_SO:SOIC-16_3.9x9.9mm_P1.27mm
- U12: value UCC27524D -> UCC27524DR
- U3, U9: value SRV05-4 -> SRV05-4HTG-D
- moved JP1 103.6 mm to (133.0, 51.7)
- moved U2 102.7 mm to (60.1, 136.2)
- moved C12 99.7 mm to (57.6, 118.5)
- moved C21 99.7 mm to (57.6, 121.5)
- moved C23 99.7 mm to (57.6, 124.5)
- moved C41 99.7 mm to (57.6, 127.5)
- moved C43 99.7 mm to (57.6, 130.5)
- moved U3 97.6 mm to (51.8, 123.3)
- moved U9 97.6 mm to (51.8, 128.0)
- moved JP2 95.7 mm to (132.3, 58.3)
- moved C63 92.9 mm to (62.4, 127.5)
- moved U11 86.1 mm to (74.6, 108.3)
- moved U12 86.1 mm to (74.6, 114.9)
- moved C24 77.3 mm to (103.6, 92.1)
- moved C49 75.8 mm to (107.6, 89.5)
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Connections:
- net Net-(RN1E-R5.2) renamed SUB_SDA
- net Net-(RN1F-R6.2) renamed SUB_SCL
- net Net-(U1-PE3) renamed SUB_led
- D8 pad 1: +12V -> ATX_PWR_o
- D9 pad 1: ATX_PWR_o -> +3.3Vdev
- U1 pad 1: Net-(U1-PE2) -> SUB_6
- U1 pad 3: Net-(U1-PE4) -> NTC_MUX_0
- U1 pad 4: Net-(U1-PE5) -> NTC_MUX_1
- U1 pad 43: Net-(RN3F-R6.1) -> Fan_2
- U1 pad 44: Net-(RN3G-R7.1) -> exrtusora
- U1 pad 45: Net-(RN3H-R8.1) -> hot_bed
- U1 pad 46: Net-(U1-PE15) -> Fan_1
- U1 pad 5: Net-(U1-PE6) -> NTC_MUX_2
- U1 pad 55: NTC_MUX_0 -> SUB_6
- U1 pad 56: NTC_MUX_1 -> SUB_5
- U1 pad 57: NTC_MUX_2 -> SUB_4
- U1 pad 58: unconnected-(U1-PD11-Pad58) -> SUB_3
- U1 pad 59: unconnected-(U1-PD12-Pad59) -> SUB_2
- U1 pad 60: unconnected-(U1-PD13-Pad60) -> SUB_1
- U1 pad 78: unconnected-(U1-PC10-Pad78) -> Net-(U1-PC10)
- U1 pad 79: unconnected-(U1-PC11-Pad79) -> Net-(U1-PC11)
- U1 pad 95: Net-(RN1D-R4.2) -> unconnected-(U1-PB8-Pad95)
- U1 pad 96: Net-(RN1C-R3.2) -> unconnected-(U1-PB9-Pad96)
- U1 pad 97: Net-(RN1A-R1.1) -> ATX_PWR_o
- U1 pad 98: Net-(RN1B-R2.1) -> MUX_EN
- U10 pad 1: NTC_ref -> NTC_driver_1
- U10 pad 12: NTC_mosfet -> NTC_mosfet_2
- U10 pad 15: NTC_driver -> NTC_mosfet_1
- U10 pad 2: Net-(J13-Pin_3) -> NTC_driver_3
- U10 pad 4: Net-(J13-Pin_5) -> NTC_driver_4
- U10 pad 5: Net-(J13-Pin_1) -> NTC_driver_2
- U10 pad 6: GND -> MUX_EN

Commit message: 05092026/00001
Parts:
- removed TH10, TH2, TH3, TH4, TH5, TH6, TH7, TH8, TH9: 10kΩ, Resistor_SMD:R_0603_1608Metric
- added C84: 100nf, Capacitor_SMD:C_0603_1608Metric, F.Cu at (123.0, 121.0)
- added R87: 4.7kΩ, Resistor_SMD:R_0603_1608Metric_Pad0.98x0.95mm_HandSolder, F.Cu at (130.0, 74.5)
- added R88: 4.7kΩ, Resistor_SMD:R_0603_1608Metric_Pad0.98x0.95mm_HandSolder, F.Cu at (130.0, 77.0)
- moved C76 49.6 mm to (123.0, 116.0)
- moved C78 49.6 mm to (123.0, 118.5)
- moved C57 44.7 mm to (119.0, 111.0)
- moved C60 44.7 mm to (119.0, 116.0)
- moved C61 44.7 mm to (119.0, 118.5)
- moved C58 44.7 mm to (119.0, 113.5)
- moved C65 44.7 mm to (119.0, 121.0)
- moved SW1 41.4 mm to (79.0, 140.7)
- moved SW2 41.4 mm to (83.6, 140.7)
- moved SW3 41.4 mm to (88.2, 140.7)
- moved C37 39.7 mm to (115.0, 111.0)
- moved C40 39.7 mm to (115.0, 118.5)
- moved C28 39.7 mm to (115.0, 106.0)
- moved C30 39.7 mm to (115.0, 108.5)
- moved C38 39.7 mm to (115.0, 113.5)
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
